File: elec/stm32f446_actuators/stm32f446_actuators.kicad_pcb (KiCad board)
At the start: 2 copper layers, 88 x 70 mm, 171 parts, among them IC1 TS2596CM550_RNG, J1 Conn_01x02, J11 1, J13 2, J15 3, J17 0, J18 4, J19 4, J2 USB_B_Micro, J21 0, J22 3, J23 1, J24 5, J25 5, J27 1, J28 4, J29 +VBAT, J3 USART, J30 2, J31 6, J32 2, J33 5, J34 +5V, J35 GND, J36 3, J37 7, J38 Conn_01x04, J39 Conn_01x04, J4 SWD, J40 0, J41 2, J42 4, J43 Conn_01x04, J44 Conn_01x04, J45 1, J46 3, J5 0, J6 Conn_01x04, J7 Conn_01x04, J8 1, J9 0, Q1 IRLZ44N, Q11 IRLZ44N, Q3 IRLZ44N, Q5 IRLZ44N, Q7 IRLZ44N, Q9 IRLZ44N, SW1 RESET, U1 MIC5504-3.3YM5, U2 STM32F103CBTx, U3 MIC5504-3.3YM5, U4 STM32F446RETx, Y1 8MHz(12pF), Y2 8MHz(16pF)[N/A]

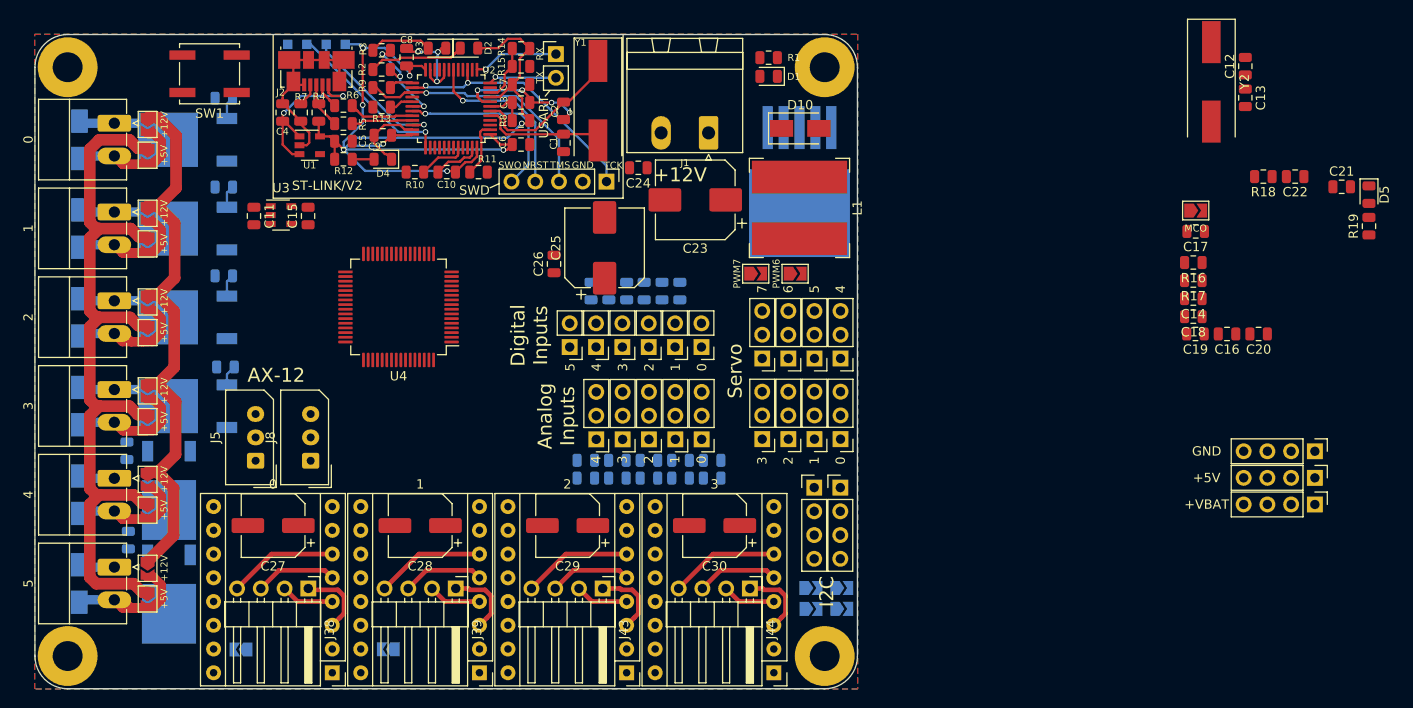
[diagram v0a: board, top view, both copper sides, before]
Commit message: Add routed PCB without GNDs and update µC sch
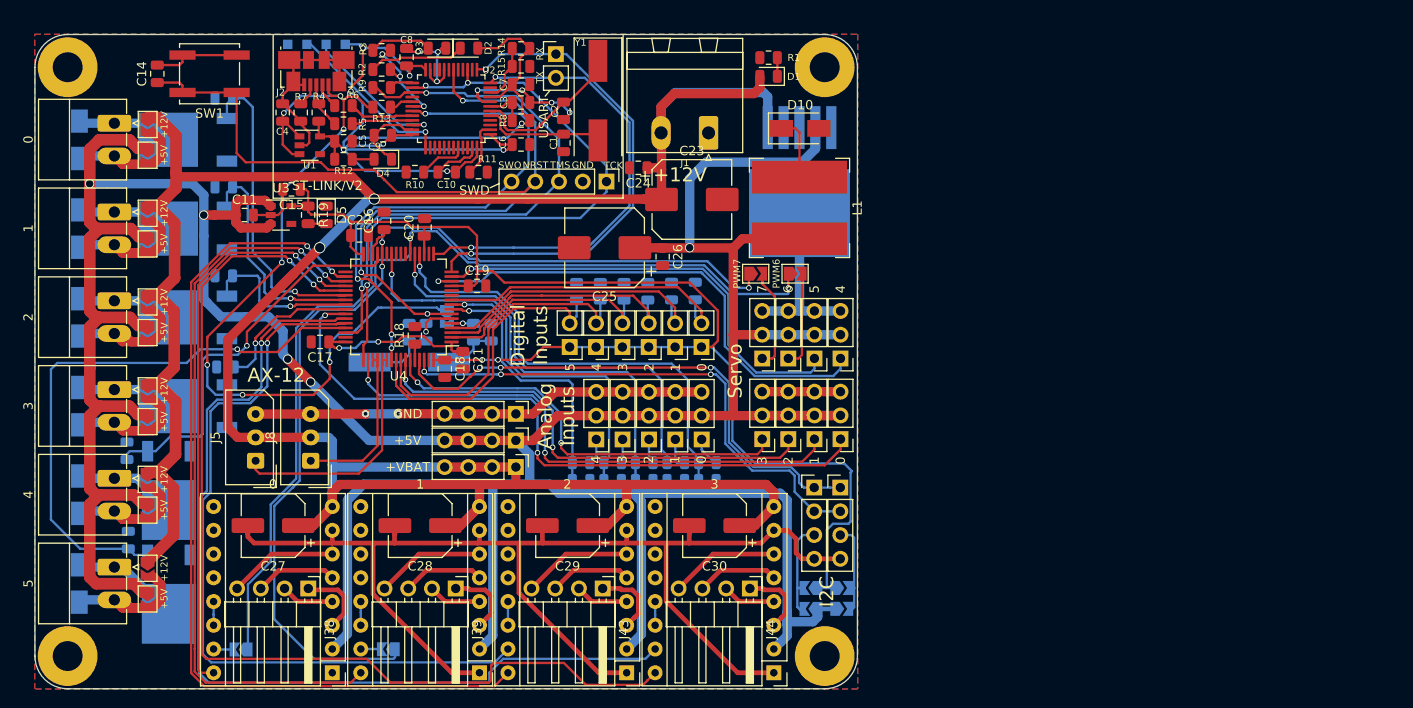
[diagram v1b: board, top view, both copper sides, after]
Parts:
- C12, C13, JP1, R16, R17, Y2: moved to B.Cu
- moved R19 113.5 mm to (79.2, 69.3), turned to 270 degrees
- moved C14 113.4 mm to (63.1, 54.2), turned to 90 degrees
- moved D5 111.6 mm to (81.2, 69.3)
- moved C22 100.3 mm to (84.7, 71.5), turned to 0 degrees
- moved C21 95.8 mm to (95.8, 84.8), turned to 270 degrees
- moved C17 94.4 mm to (80.5, 82.9)
- moved C13 92.9 mm to (90.0, 81.8), turned to 90 degrees
- moved R18 92.4 mm to (90.7, 82.2), turned to 90 degrees
- moved C16 91.0 mm to (87.4, 69.9), turned to 90 degrees
- moved Y2 90.9 mm to (90.1, 85.1), turned to 180 degrees
- moved C20 90.0 mm to (91.7, 70.6), turned to 90 degrees
- moved J29 85.6 mm to (101.5, 96.3)
- moved J34 85.6 mm to (101.5, 93.4)
- moved J35 85.6 mm to (101.5, 90.6)
- moved C12 85.6 mm to (98.8, 81.8)
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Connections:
- U4 pad 10: /Actuators/DigitalIn4 -> /Actuators/DigitalIn0
- U4 pad 11: /Actuators/DigitalIn5 -> /STM32F446RE6/DigitalOut7
- U4 pad 14: /Actuators/PWM7 -> /Actuators/PWM4
- U4 pad 15: /Actuators/PWM14 -> /Actuators/PWM5
- U4 pad 2: /Actuators/DigitalIn2 -> /Actuators/DigitalIn3
- U4 pad 20: /Actuators/AnalogIn1 -> /Actuators/AnalogIn0
- U4 pad 21: /Actuators/AnalogIn4 -> /Actuators/AnalogIn1
- U4 pad 23: /Actuators/DigitalOut1 -> /STM32F446RE6/DigitalOut6
- U4 pad 27: /Actuators/DigitalOut3 -> /STM32F446RE6/DigitalOut10
- U4 pad 28: /Actuators/PWM13 -> /Actuators/PWM7
- U4 pad 29: /Actuators/PWM5 -> /Actuators/PWM14
- U4 pad 3: /Actuators/DigitalIn3 -> /Actuators/DigitalIn2
- U4 pad 33: /Actuators/DigitalOut4 -> /STM32F446RE6/DigitalOut5
- U4 pad 34: /STM32F446RE6/DigitalOut5 -> /Actuators/DigitalOut2
- U4 pad 35: /STM32F446RE6/DigitalOut6 -> /Actuators/DigitalOut1
- U4 pad 36: /STM32F446RE6/DigitalOut7 -> /Actuators/DigitalOut0
- U4 pad 37: /STM32F446RE6/DigitalOut10 -> /Actuators/DigitalOut3
- U4 pad 38: /Actuators/PWM4 -> /Actuators/PWM10
- U4 pad 39: /Actuators/PWM12 -> /Actuators/PWM11
- U4 pad 4: /Actuators/DigitalOut0 -> /Actuators/DigitalIn1
- U4 pad 40: /Actuators/PWM0 -> /Actuators/PWM12
- U4 pad 41: /Actuators/PWM8 -> /Actuators/PWM13
- U4 pad 42: /Actuators/PWM1 -> /Actuators/PWM0
- U4 pad 44: /Actuators/PWM2 -> /Actuators/PWM8
- U4 pad 45: /Actuators/DigitalOut2 -> /Actuators/DigitalOut4
- U4 pad 50: /Actuators/PWM10 -> /Actuators/PWM1
- U4 pad 51: /Actuators/RX3 -> /Actuators/RX5
- U4 pad 52: /Actuators/RX3 -> /Actuators/RX5
- U4 pad 53: /Actuators/RX5 -> /Actuators/RX3
- U4 pad 54: /Actuators/RX5 -> /Actuators/RX3
- U4 pad 56: /Actuators/DigitalIn0 -> /Actuators/DigitalIn5
- U4 pad 57: /Actuators/DigitalIn1 -> /Actuators/DigitalIn4
- U4 pad 58: /Actuators/PWM11 -> /Actuators/PWM2
- U4 pad 8: /Actuators/AnalogIn0 -> /Actuators/AnalogIn4
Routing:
- net +5V: track 103.7 -> 428.8 mm, vias 2 -> 7
- net +12V: track 61.0 -> 303.8 mm, vias 0 -> 2
- net GND: track 61.6 -> 295.9 mm, vias 7 -> 9
- net +3V3: track 0.00 -> 164.3 mm, vias 0 -> 4
- net /Actuators/DigitalOut3: track 0.00 -> 110.7 mm, vias 0 -> 2
- net /Actuators/PWM7: track 0.00 -> 107.9 mm, vias 0 -> 3
- net /Actuators/PWM6: track 0.00 -> 103.1 mm, vias 0 -> 2
- net /Actuators/PWM9: track 0.00 -> 101.7 mm, vias 0 -> 1
- net /Actuators/DigitalOut2: track 0.00 -> 96.6 mm, vias 0 -> 2
- net /STM32F446RE6/NRST: track 18.8 -> 105.9 mm, vias 1 -> 3
- net /Actuators/PWM8: track 0.00 -> 82.2 mm, vias 0 -> 1
- net /Actuators/DigitalOut1: track 0.00 -> 79.4 mm, vias 0 -> 2
- net /Actuators/PWM0: track 0.00 -> 73.5 mm, vias 0 -> 2
- net /STM32F446RE6/MCO: track 0.00 -> 72.6 mm, vias 0 -> 5
- net /Actuators/DigitalOut0: track 0.00 -> 61.7 mm, vias 0 -> 2
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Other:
- net class Default: clearance 0.2 -> 0.127
- rule trace_clearance: 0.2 -> 0.127

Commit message: GND done, silkscreen done and some minor fixes
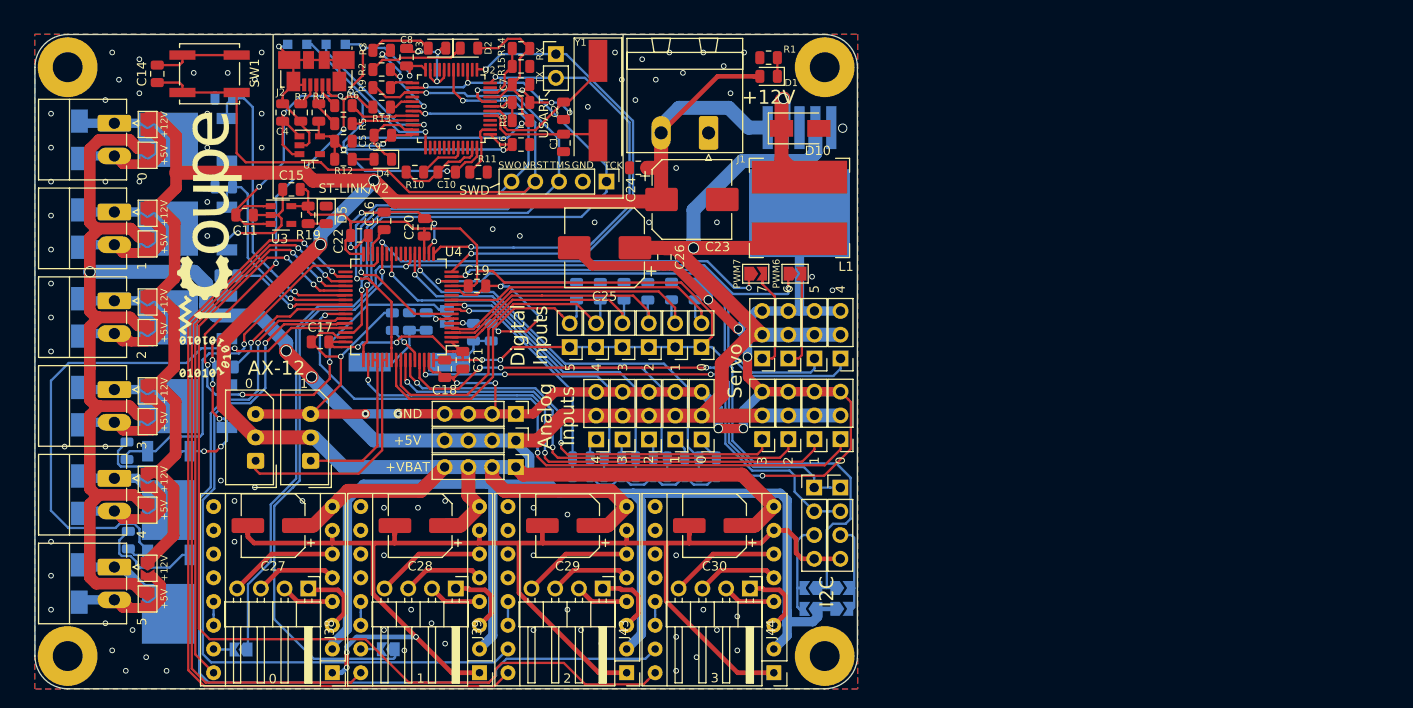
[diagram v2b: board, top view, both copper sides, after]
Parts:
- added G***: LOGO, villanut_lib:logo_UTCoupe_Medium, F.Cu at (68.6, 72.6)
- R18: moved to B.Cu
- moved R18 2.82 mm to (88.2, 80.7)
- moved C13 1.14 mm to (90.1, 80.7)
- moved R17 1.14 mm to (91.9, 80.7)
- moved R39 0.51 mm to (115.2, 97.2)
- moved R40 0.51 mm to (108.5, 97.2)
- moved R42 0.51 mm to (115.2, 95.3)
- moved R43 0.51 mm to (108.5, 95.3)
- moved R44 0.51 mm to (118.6, 97.2)
- moved R45 0.51 mm to (111.8, 97.2)
- moved R46 0.51 mm to (118.6, 95.3)
- moved R47 0.51 mm to (111.8, 95.3)
- moved R38 0.51 mm to (122.0, 97.2)
- moved R41 0.51 mm to (122.0, 95.3)
- moved R24 0.43 mm to (70.6, 75.8)
- moved C26 0.19 mm to (117.3, 73.8)
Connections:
- C11 pad 1: +5V -> VBUS
- C4 pad 1: +5V -> VBUS
- J2 pad 1: +5V -> VBUS
- U1 pad 1: +5V -> VBUS
- U1 pad 3: +5V -> VBUS
- U3 pad 1: +5V -> VBUS
- U3 pad 3: +5V -> VBUS
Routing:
- net GND: track 295.9 -> 540.8 mm, vias 9 -> 123
- net +5V: track 428.8 -> 382.6 mm, vias 7 -> 4
- net VBUS: track 0.00 -> 38.6 mm, vias 0 -> 3
- net +12V: track 303.8 -> 297.2 mm
- net Net-(D10-Pad1): track 6.88 -> 12.4 mm, vias 0 -> 1
- net /Actuators/PWM6: track 103.1 -> 98.1 mm
- net /Actuators/AnalogIn2: track 47.5 -> 42.7 mm
- net /Actuators/AnalogIn0: track 49.8 -> 45.5 mm
- net /Actuators/DigitalOut3: track 110.7 -> 106.5 mm
- net /Actuators/AnalogIn3: track 33.8 -> 30.2 mm
- net /Actuators/AnalogIn4: track 29.1 -> 25.6 mm
- net /Actuators/DigitalOut0: track 61.7 -> 59.1 mm
- net /Actuators/DigitalOut4: track 61.6 -> 64.1 mm
- net /STM32F446RE6/PH1: track 5.50 -> 2.99 mm
- net Net-(R18-Pad1): track 1.69 -> 4.19 mm, vias 0 -> 1
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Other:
- board text added: "Actuators V1.0"
- board text added: "CDR 2020"
- board text added: "Program ST-LINK/V2"
- board text removed: "Program"

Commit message: Add step file, bom, pdf schematic
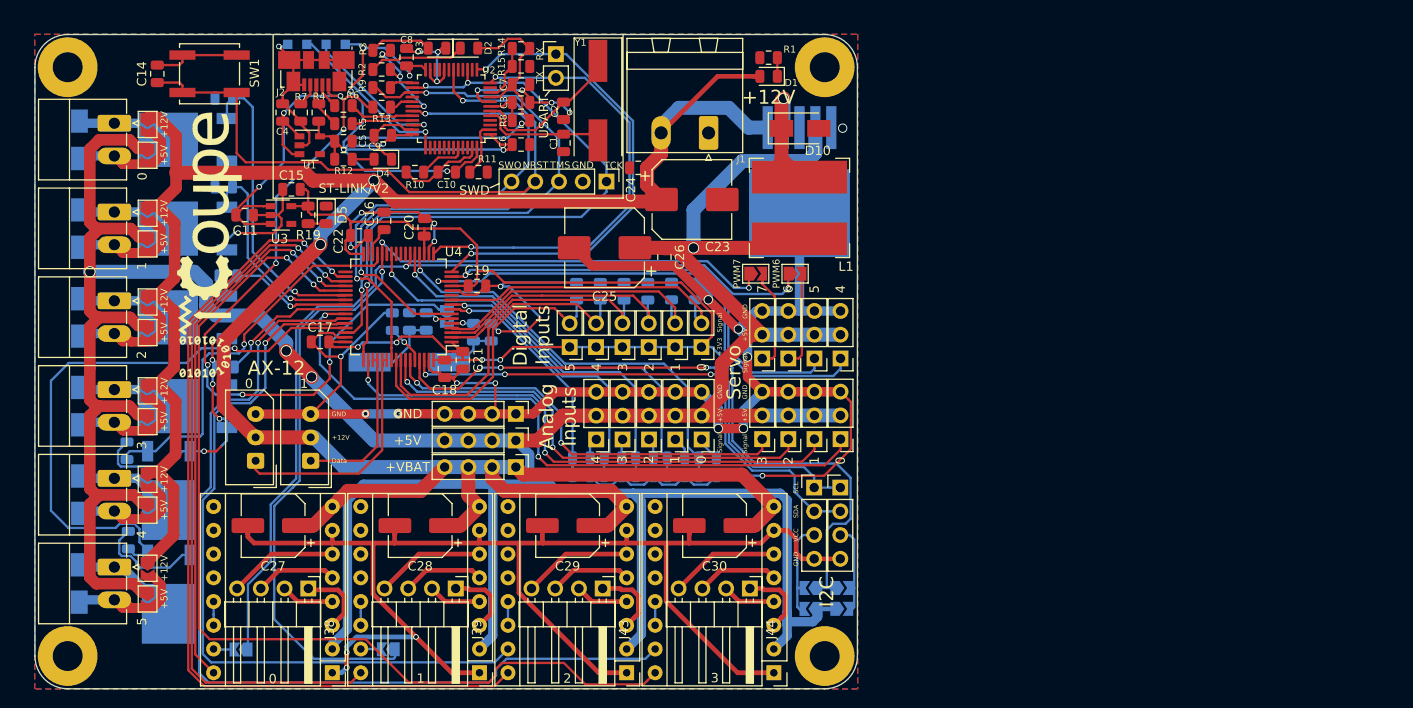
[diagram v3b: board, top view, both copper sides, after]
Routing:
- net GND: vias 123 -> 35
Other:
- board text added: "+3V3"
- board text added: "+5V"
- board text added: "Data"
- board text added: "SCL"
- board text added: "SDA"
- board text added: "Signal"
- board text added: "VCC"
